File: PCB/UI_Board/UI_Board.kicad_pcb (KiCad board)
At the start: 2 copper layers, 143.2 x 35 mm, 15 parts, among them J1 DISPLAY, J2 CABLE, SW1 SW_UP, SW2 SW_DWN, SW3 SW_PRE_1, SW4 SW_PRE_2

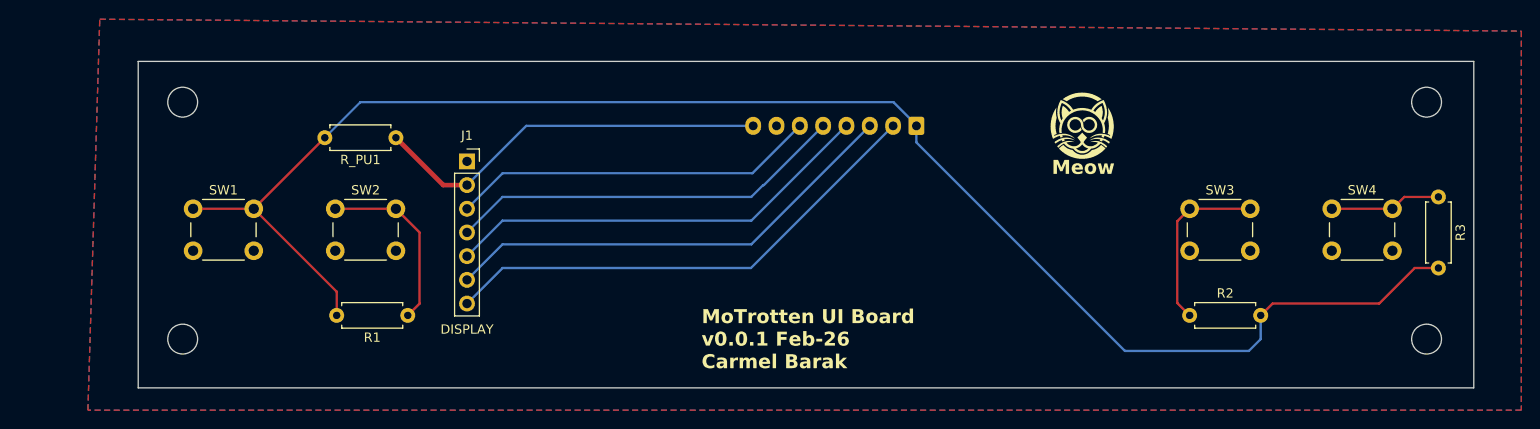
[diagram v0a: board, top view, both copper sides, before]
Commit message: Updated boards and added DRU files
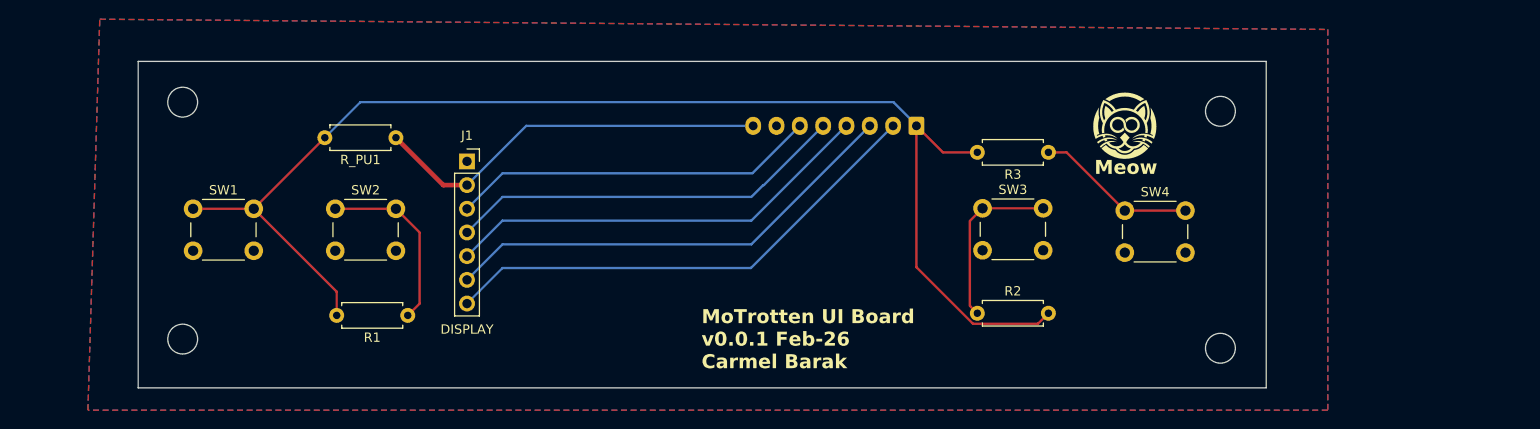
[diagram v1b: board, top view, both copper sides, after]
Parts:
- moved R3 42.1 mm to (156.3, 44.8), turned to 180 degrees
- moved R2 22.8 mm to (148.7, 62.0)
- moved SW3 22.2 mm to (149.2, 50.8)
- moved SW4 22.2 mm to (164.5, 51.0)
- moved H1 22.1 mm to (174.8, 40.4)
- moved H3 22.1 mm to (174.8, 65.8)
- moved ? 4.57 mm to (167.4, 40.1)
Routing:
- net /BTNS: track 170.7 -> 138.5 mm
- net Net-(R3-Pad1): track 12.0 -> 17.3 mm
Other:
- board size 143.2 x 35 mm -> 120.9 x 35 mm
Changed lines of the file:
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@@
 	(footprint "Button_Switch_THT:SW_PUSH_6mm"
 		(layer "F.Cu")
-		(at 186.69 50.8)
+		(at 164.5 51)
 		(descr "Generic 6mm SW tactile push button")
 		(tags "tact sw push 6mm")
@@
 	(footprint "MountingHole:MountingHole_3.2mm_M3"
 		(layer "F.Cu")
-		(at 196.85 64.77)
+		(at 174.75 65.75)
 		(descr "Mounting Hole 3.2mm, M3, no annular, generated by kicad-footprint-generator mountinghole.py")
 		(tags "mountinghole M3")
@@
 	(footprint "MountingHole:MountingHole_3.2mm_M3"
 		(layer "F.Cu")
-		(at 196.85 39.37)
+		(at 174.75 40.35)
 		(descr "Mounting Hole 3.2mm, M3, no annular, generated by kicad-footprint-generator mountinghole.py")
 		(tags "mountinghole M3")
@@
 	)
 	(footprint "clipboard:13b59317-ab6f-4fc0-bdb4-4b3abb5c9487"
+		(locked yes)
 		(layer "F.Cu")
-		(at 162.814 40.132)
+		(at 167.383054 40.132)
 		(property "Reference" ""
 			(at 0 0 0)
@@
 	(footprint "Button_Switch_THT:SW_PUSH_6mm"
 		(layer "F.Cu")
-		(at 171.45 50.8)
+		(at 149.25 50.75)
 		(descr "Generic 6mm SW tactile push button")
 		(tags "tact sw push 6mm")
@@
 	(footprint "Resistor_THT:R_Axial_DIN0207_L6.3mm_D2.5mm_P7.62mm_Horizontal"
 		(layer "F.Cu")
-		(at 171.45 62.23)
+		(at 148.69 62)
 		(descr "Resistor, Axial_DIN0207 series, Axial, Horizontal, pin pitch=7.62mm, 0.25W = 1/4W, length*diameter=6.3*2.5mm^2, http://cdn-reichelt.de/documents/datenblatt/B400/1_4W%23YAG.pdf")
 		(tags "Resistor Axial_DIN0207 series Axial Horizontal pin pitch 7.62mm 0.25W = 1/4W length 6.3mm diameter 2.5mm")
@@
 	(footprint "Resistor_THT:R_Axial_DIN0207_L6.3mm_D2.5mm_P7.62mm_Horizontal"
 		(layer "F.Cu")
-		(at 198.12 49.53 -90)
+		(at 156.31 44.75 180)
 		(descr "Resistor, Axial_DIN0207 series, Axial, Horizontal, pin pitch=7.62mm, 0.25W = 1/4W, length*diameter=6.3*2.5mm^2, http://cdn-reichelt.de/documents/datenblatt/B400/1_4W%23YAG.pdf")
 		(tags "Resistor Axial_DIN0207 series Axial Horizontal pin pitch 7.62mm 0.25W = 1/4W length 6.3mm diameter 2.5mm")
 		(property "Reference" "R3"
-			(at 3.81 -2.37 90)
+			(at 3.81 -2.37 0)
 			(layer "F.SilkS")
 			(effects
@@
 		)
 		(property "Value" "4.7K"
-			(at 3.81 2.37 90)
+			(at 3.81 2.37 0)
 			(layer "F.Fab")
 			(effects
@@
 		)
 		(property "Datasheet" "~"
-			(at 0 0 90)
+			(at 0 0 0)
 			(layer "F.Fab")
 			(hide yes)
@@
 		)
 		(property "Description" "Resistor"
-			(at 0 0 90)
+			(at 0 0 0)
 			(layer "F.Fab")
 			(hide yes)
@@
 		(attr through_hole)
 		(fp_line
-			(start 0.54 1.37)
-			(end 7.08 1.37)
+			(start 7.08 1.37)
+			(end 7.08 1.04)
 			(stroke
 				(width 0.12)
@@
 		)
 		(fp_line
-			(start 7.08 1.37)
-			(end 7.08 1.04)
+			(start 7.08 -1.37)
+			(end 7.08 -1.04)
 			(stroke
 				(width 0.12)
@@
 		)
 		(fp_line
-			(start 0.54 1.04)
-			(end 0.54 1.37)
+			(start 0.54 1.37)
+			(end 7.08 1.37)
 			(stroke
 				(width 0.12)
@@
 		)
 		(fp_line
-			(start 0.54 -1.04)
-			(end 0.54 -1.37)
+			(start 0.54 1.04)
+			(end 0.54 1.37)
 			(stroke
 				(width 0.12)
@@
 		)
 		(fp_line
-			(start 0.54 -1.37)
-			(end 7.08 -1.37)
+			(start 0.54 -1.04)
+			(end 0.54 -1.37)
 			(stroke
 				(width 0.12)
@@
 		)
 		(fp_line
-			(start 7.08 -1.37)
-			(end 7.08 -1.04)
+			(start 0.54 -1.37)
+			(end 7.08 -1.37)
 			(stroke
 				(width 0.12)
@@
 		)
 		(fp_line
-			(start 0 0)
-			(end 0.66 0)
+			(start 7.62 0)
+			(end 6.96 0)
 			(stroke
 				(width 0.1)
@@
 		)
 		(fp_line
-			(start 7.62 0)
-			(end 6.96 0)
+			(start 0 0)
+			(end 0.66 0)
 			(stroke
 				(width 0.1)
@@
 		)
 		(fp_text user "${REFERENCE}"
-			(at 3.81 0 90)
+			(at 3.81 0 0)
 			(layer "F.Fab")
 			(effects
@@
 		)
 		(pad "1" thru_hole circle
-			(at 0 0 270)
+			(at 0 0 180)
 			(size 1.6 1.6)
 			(drill 0.8)
@@
 		)
 		(pad "2" thru_hole circle
-			(at 7.62 0 270)
+			(at 7.62 0 180)
 			(size 1.6 1.6)
 			(drill 0.8)
@@
 	(gr_rect
 		(start 58.73 35)
-		(end 201.91 70)
+		(end 179.66 70)
 		(stroke
 			(width 0.05)
@@
 	)
 	(gr_text "Meow"
-		(at 156.66666 47.244 0)
+		(locked yes)
+		(at 161.235714 47.244 0)
 		(layer "F.SilkS")
 		(effects
@@
 	)
 	(segment
+		(start 155.184 63.126)
+		(end 148.223595 63.126)
+		(width 0.25)
+		(layer "F.Cu")
+		(net 8)
+	)
+	(segment
 		(start 71.12 50.8)
 		(end 80.01 59.69)
@@
 	)
 	(segment
-		(start 80.01 59.69)
-		(end 80.01 62.23)
+		(start 148.69 44.75)
+		(end 145 44.75)
 		(width 0.25)
 		(layer "F.Cu")
@@
 	)
 	(segment
-		(start 191.77 60.96)
-		(end 180.34 60.96)
+		(start 80.01 59.69)
+		(end 80.01 62.23)
 		(width 0.25)
 		(layer "F.Cu")
@@
 	)
 	(segment
-		(start 198.12 57.15)
-		(end 195.58 57.15)
+		(start 156.31 62)
+		(end 155.184 63.126)
 		(width 0.25)
 		(layer "F.Cu")
@@
 	)
 	(segment
-		(start 180.34 60.96)
-		(end 179.07 62.23)
+		(start 148.223595 63.126)
+		(end 142.16 57.062405)
 		(width 0.25)
 		(layer "F.Cu")
@@
 	)
 	(segment
-		(start 195.58 57.15)
-		(end 191.77 60.96)
+		(start 145 44.75)
+		(end 142.16 41.91)
 		(width 0.25)
 		(layer "F.Cu")
@@
 	)
 	(segment
-		(start 78.74 43.18)
-		(end 71.12 50.8)
+		(start 142.16 57.062405)
+		(end 142.16 41.91)
 		(width 0.25)
 		(layer "F.Cu")
@@
 	)
 	(segment
-		(start 177.8 66.04)
-		(end 179.07 64.77)
+		(start 78.74 43.18)
+		(end 71.12 50.8)
 		(width 0.25)
-		(layer "B.Cu")
+		(layer "F.Cu")
 		(net 8)
 	)
@@
 	)
 	(segment
-		(start 179.07 64.77)
-		(end 179.07 62.23)
-		(width 0.25)
-		(layer "B.Cu")
-		(net 8)
-	)
-	(segment
-		(start 164.509728 66.04)
-		(end 177.8 66.04)
-		(width 0.25)
-		(layer "B.Cu")
-		(net 8)
-	)
-	(segment
 		(start 78.74 43.18)
 		(end 82.55 39.37)
@@
 	)
 	(segment
-		(start 142.16 41.91)
-		(end 142.16 43.690272)
-		(width 0.25)
-		(layer "B.Cu")
-		(net 8)
-	)
-	(segment
 		(start 139.7 39.37)
 		(end 142.16 41.83)
@@
 	)
 	(segment
-		(start 142.16 43.690272)
-		(end 164.509728 66.04)
-		(width 0.25)
-		(layer "B.Cu")
-		(net 8)
-	)
-	(segment
 		(start 86.36 50.8)
 		(end 79.86 50.8)
@@
 	)
 	(segment
-		(start 177.95 50.8)
-		(end 171.45 50.8)
+		(start 148.69 62)
+		(end 147.890001 61.200001)
 		(width 0.25)
 		(layer "F.Cu")
@@
 	)
 	(segment
-		(start 170.124 60.904)
-		(end 170.124 52.126)
+		(start 147.890001 61.200001)
+		(end 147.890001 52.109999)
 		(width 0.25)
 		(layer "F.Cu")
@@
 	)
 	(segment
-		(start 170.124 52.126)
-		(end 171.45 50.8)
+		(start 147.890001 52.109999)
+		(end 149.25 50.75)
 		(width 0.25)
 		(layer "F.Cu")
@@
 	)
 	(segment
-		(start 171.45 62.23)
-		(end 170.124 60.904)
+		(start 155.75 50.75)
+		(end 149.25 50.75)
 		(width 0.25)
 		(layer "F.Cu")
@@
 	)
 	(segment
-		(start 194.46 49.53)
-		(end 193.19 50.8)
+		(start 156.31 44.75)
+		(end 158.25 44.75)
 		(width 0.25)
 		(layer "F.Cu")
@@
 	)
 	(segment
-		(start 186.69 50.8)
-		(end 193.19 50.8)
+		(start 171 51)
+		(end 164.5 51)
 		(width 0.25)
 		(layer "F.Cu")
@@
 	)
 	(segment
-		(start 198.12 49.53)
-		(end 194.46 49.53)
+		(start 158.25 44.75)
+		(end 164.5 51)
 		(width 0.25)
 		(layer "F.Cu")
@@
 		(polygon
 			(pts
-				(xy 207.01 31.75) (xy 207.01 72.39) (xy 53.34 72.39) (xy 54.61 30.48)
+				(xy 186.26 31.577083) (xy 186.26 72.39) (xy 53.34 72.39) (xy 54.61 30.48)
 			)
 		)
 	)
+	(group ""
+		(locked yes)
+		(members "d7ff63a6-8589-4dde-9ec1-a1ef15ab59fa" "e704f8f9-859c-49a1-b126-25c3881b70f6")
+	)
 	(embedded_fonts no)

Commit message: Updated boards
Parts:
- removed R_PU1: 10K, Resistor_THT:R_Axial_DIN0207_L6.3mm_D2.5mm_P7.62mm_Horizontal
- moved R3 29.3 mm to (180.3, 61.5)
- moved R2 29.0 mm to (173.2, 46.5)
- moved SW4 19.8 mm to (184.2, 51.2)
- moved H3 19.3 mm to (194.0, 65.5)
- moved H1 18.8 mm to (193.5, 40.0)
- moved R1 16.1 mm to (71.8, 59.5)
- moved SW3 13.0 mm to (162.2, 51.1)
- moved SW1 11.4 mm to (53.2, 51.1)
- moved J2 11.4 mm to (130.8, 41.5)
- moved H4 10.5 mm to (53.0, 65.5)
- moved H2 10.5 mm to (53.0, 39.4)
- moved SW2 4.62 mm to (75.2, 51.1)
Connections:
- J2 pad 1: /BTNS -> /3V3
- J2 pad 2: /CS -> GND
- J2 pad 3: /DC -> /CS
- J2 pad 4: /RST -> /SDA
- J2 pad 5: /SDA -> /SCL
- J2 pad 6: /SCL -> /RST
- J2 pad 7: GND -> /DC
- J2 pad 8: /3V3 -> /BTNS
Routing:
- net /BTNS: track 138.5 -> 164.8 mm
- net /CS: track 53.6 -> 39.9 mm
- net /SCL: track 39.4 -> 30.7 mm
- net /SDA: track 42.9 -> 34.2 mm
- net /DC: track 50.0 -> 41.7 mm
- net /RST: track 46.5 -> 39.8 mm
- net Net-(R2-Pad1): track 18.6 -> 12.9 mm
- net Net-(R1-Pad1): track 19.5 -> 16.3 mm
- net /3V3: track 43.0 -> 41.4 mm
- net Net-(R3-Pad1): track 17.3 -> 18.4 mm
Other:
- board size 120.9 x 35 mm -> 149.4 x 35 mm
- board text removed: "MoTrotten UI Board v0.0.1 Feb-26 Carmel Barak"
